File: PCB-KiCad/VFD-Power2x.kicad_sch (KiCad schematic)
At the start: 17 parts

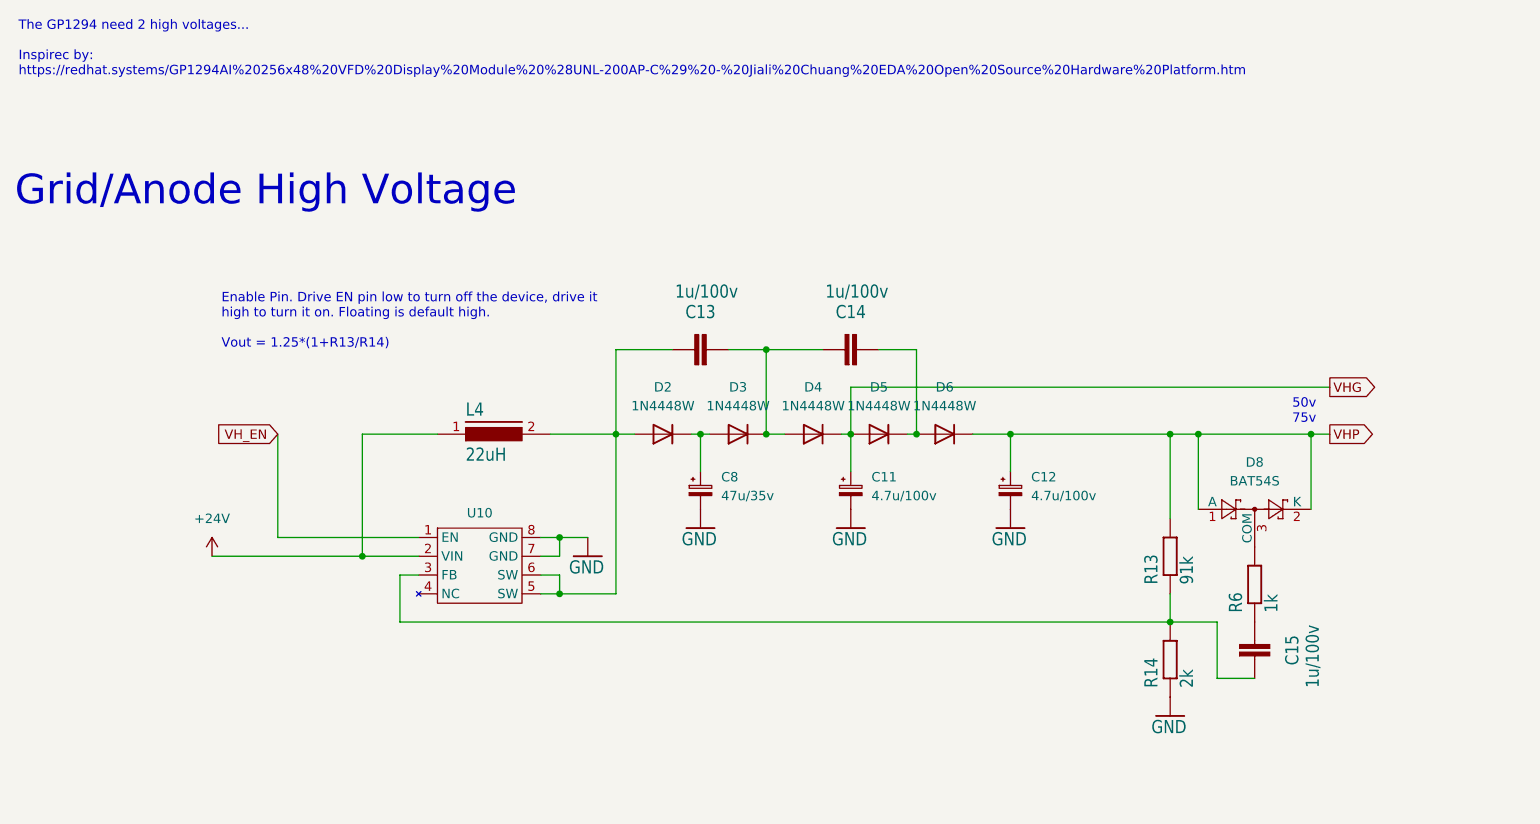
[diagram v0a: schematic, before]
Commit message: GP1294 board, added light and remote sensors.
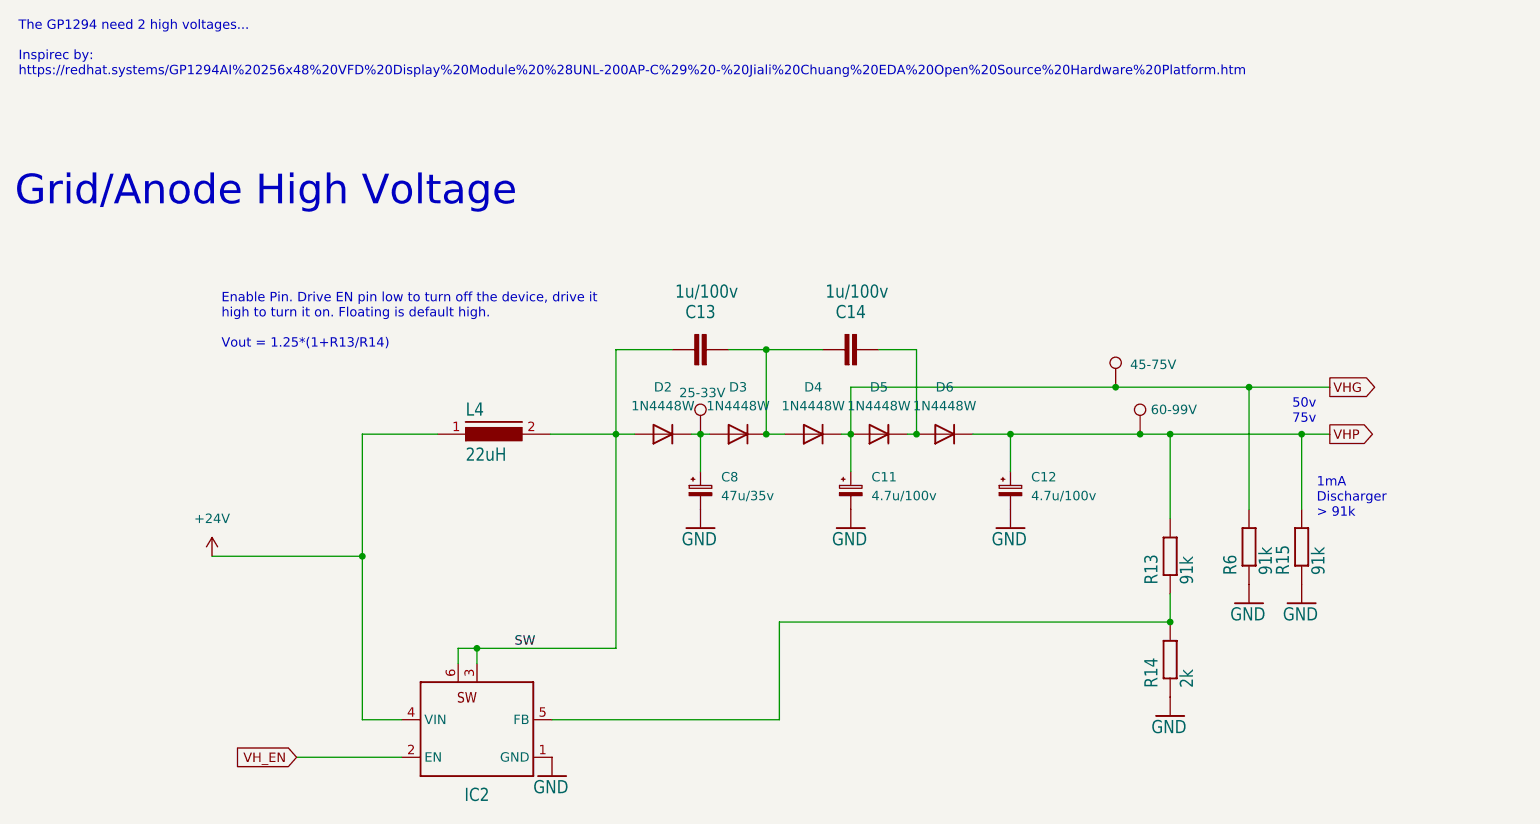
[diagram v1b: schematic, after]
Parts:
- removed C15: 1u/100v, VFD-Power:C1206, symbol VFD-Power:C-EUC1206
- removed D8: BAT54S, Package_TO_SOT_SMD:SOT-23, symbol Diode:BAT54S
- removed U10: ~, VFD-Power:SO8, symbol VFD-Power:XL6007
- added IC2: ~, VFD-Power:TO263-5, symbol VFD-Power:XL6009
- added R15: 91k, VFD-Power:R1206, symbol VFD-Power-eagle-import:R-EU_R1206
- added TP1: 45-75V, TestPoint:TestPoint_Pad_2.0x2.0mm, symbol Connector:TestPoint
- added TP16: 25-33V, TestPoint:TestPoint_Pad_2.0x2.0mm, symbol Connector:TestPoint
- added TP9: 60-99V, TestPoint:TestPoint_Pad_2.0x2.0mm, symbol Connector:TestPoint
- R6: value 1k -> 91k
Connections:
- net +24V: now also IC2.4 (VIN)
- net GND: now also R6.1, IC2.1 (GND), R15.1
- net VHG: now also R6.2, TP1.1
- net VHP: now also R15.2, TP9.1
- net VH_EN: now also IC2.2 (EN)
- net at C8.1, D2.1 (K), D3.2 (A): now also TP16.1
- net at R13.1, R14.2: now also IC2.5 (FB)
- net SW: now reaches C13.1, D2.2 (A), L4.2
- net SW: now also IC2.3 (SW), IC2.6 (SW@1)
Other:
- note added: "1mA Discharger > 91k"
